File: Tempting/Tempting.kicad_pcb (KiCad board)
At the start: 2 copper layers, 50 parts, among them J1 Conn_Coaxial, J2 Conn_01x07_Socket, J3 Conn_ARM_SWD_TagConnect_TC2030, J4 USB_C_Receptacle_USB2.0_16P, SW1 SPST, SW2 SPST, U1 AMS1117-3.3, U2 SCD41-D-R2, U3 STM32WB55CGUx, U4 DPS368, U5 USBLC6-2SC6, X1 32M, X2 32.768k

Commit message: Added net classes
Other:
- copper layers 2 -> 4
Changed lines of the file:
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@@
 	(generator_version "8.0")
 	(general
-		(thickness 1.6)
+		(thickness 1.5842)
 		(legacy_teardrops no)
 	)
@@
 	(layers
 		(0 "F.Cu" signal)
+		(1 "In1.Cu" signal)
+		(2 "In2.Cu" signal)
 		(31 "B.Cu" signal)
-		(32 "B.Adhes" user "B.Adhesive")
-		(33 "F.Adhes" user "F.Adhesive")
 		(34 "B.Paste" user)
 		(35 "F.Paste" user)
@@
 		(38 "B.Mask" user)
 		(39 "F.Mask" user)
-		(40 "Dwgs.User" user "User.Drawings")
-		(41 "Cmts.User" user "User.Comments")
-		(42 "Eco1.User" user "User.Eco1")
-		(43 "Eco2.User" user "User.Eco2")
 		(44 "Edge.Cuts" user)
 		(45 "Margin" user)
 		(46 "B.CrtYd" user "B.Courtyard")
 		(47 "F.CrtYd" user "F.Courtyard")
-		(48 "B.Fab" user)
-		(49 "F.Fab" user)
-		(50 "User.1" user)
-		(51 "User.2" user)
-		(52 "User.3" user)
-		(53 "User.4" user)
-		(54 "User.5" user)
-		(55 "User.6" user)
-		(56 "User.7" user)
-		(57 "User.8" user)
-		(58 "User.9" user)
 	)
 	(setup
+		(stackup
+			(layer "F.SilkS"
+				(type "Top Silk Screen")
+			)
+			(layer "F.Paste"
+				(type "Top Solder Paste")
+			)
+			(layer "F.Mask"
+				(type "Top Solder Mask")
+				(thickness 0.01)
+			)
+			(layer "F.Cu"
+				(type "copper")
+				(thickness 0.035)
+			)
+			(layer "dielectric 1"
+				(type "prepreg")
+				(thickness 0.0994)
+				(material "3313")
+				(epsilon_r 4.5)
+				(loss_tangent 0.02)
+			)
+			(layer "In1.Cu"
+				(type "copper")
+				(thickness 0.0152)
+			)
+			(layer "dielectric 2"
+				(type "core")
+				(color "FR4 natural")
+				(thickness 1.265)
+				(material "FR4")
+				(epsilon_r 4.5)
+				(loss_tangent 0.02)
+			)
+			(layer "In2.Cu"
+				(type "copper")
+				(thickness 0.0152)
+			)
+			(layer "dielectric 3"
+				(type "prepreg")
+				(thickness 0.0994)
+				(material "3313")
+				(epsilon_r 4.5)
+				(loss_tangent 0.02)
+			)
+			(layer "B.Cu"
+				(type "copper")
+				(thickness 0.035)
+			)
+			(layer "B.Mask"
+				(type "Bottom Solder Mask")
+				(thickness 0.01)
+			)
+			(layer "B.Paste"
+				(type "Bottom Solder Paste")
+			)
+			(layer "B.SilkS"
+				(type "Bottom Silk Screen")
+			)
+			(copper_finish "HAL lead-free")
+			(dielectric_constraints yes)
+		)
 		(pad_to_mask_clearance 0)
 		(allow_soldermask_bridges_in_footprints no)

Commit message: Rough initial layout
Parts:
- added C23: 10u, Capacitor_SMD:C_0805_2012Metric, F.Cu at (110.5, 48.6)
- added C24: 100n, Capacitor_SMD:C_0402_1005Metric, F.Cu at (112.5, 77.5)
- added C25: 100n, Capacitor_SMD:C_0402_1005Metric, F.Cu at (125.5, 77.5)
- C10, C12: value 100n -> 4.7u; footprint Capacitor_SMD:C_0402_1005Metric -> Capacitor_SMD:C_0603_1608Metric
- C11: value C -> 100n
- C13: value 100n -> C
- C17: value 4.7u -> 100n; footprint Capacitor_SMD:C_0603_1608Metric -> Capacitor_SMD:C_0402_1005Metric
- C20: value 10u -> 4.7u; footprint Capacitor_SMD:C_0805_2012Metric -> Capacitor_SMD:C_0603_1608Metric
- moved SW2 99.3 mm to (128.5, 81.8), turned to 180 degrees
- moved FLT1 95.5 mm to (131.9, 60.5)
- moved J2 93.5 mm to (126.1, 45.6), turned to -90 degrees
- moved C6 87.3 mm to (128.5, 63.0), turned to 90 degrees
- moved X1 86.9 mm to (123.8, 52.1)
- moved SW1 86.0 mm to (110.3, 81.8), turned to 180 degrees
- moved R5 84.7 mm to (127.0, 48.6), turned to 180 degrees
- moved L1 84.2 mm to (126.1, 60.5)
- moved C3 84.0 mm to (124.6, 63.0), turned to 90 degrees
- moved U4 82.9 mm to (118.5, 75.5), turned to 90 degrees
- moved C8 82.9 mm to (124.5, 61.1), turned to -90 degrees
- moved J1 82.3 mm to (136.1, 61.0)
- moved C10 81.3 mm to (125.3, 37.7), turned to 90 degrees
- moved R2 81.1 mm to (123.0, 68.5)
- moved C15 80.9 mm to (127.5, 38.3), turned to 90 degrees
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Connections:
- net /MCU_SMPSFB renamed /SMPSFB_MCU
- net /MCU_SMPSLX renamed /SMPSLX_MCU
- net Net-(D1-BK) renamed /LED_B
- net Net-(D1-GK) renamed /LED_G
- net Net-(D1-RK) renamed /LED_R
- net Net-(U3-PA0) renamed /LED_R_MCU
- net Net-(U3-PA1) renamed /LED_G_MCU
- net Net-(U3-PA2) renamed /LED_B_MCU
- C11 pad 1: /LSE_OUT -> +3.3V
- C13 pad 1: +3.3V -> /LSE_OUT
- C21 pad 1: /BUTTON_1 -> +3.3V
- C22 pad 1: /BUTTON_2 -> +3.3V
- SW1 pad 2: unconnected-(SW1-Pad2) -> GND
- SW1 pad 3: unconnected-(SW1-K-Pad3) -> /BUTTON_1
- SW2 pad 2: unconnected-(SW2-Pad2) -> GND
- SW2 pad 3: unconnected-(SW2-K-Pad3) -> /BUTTON_2

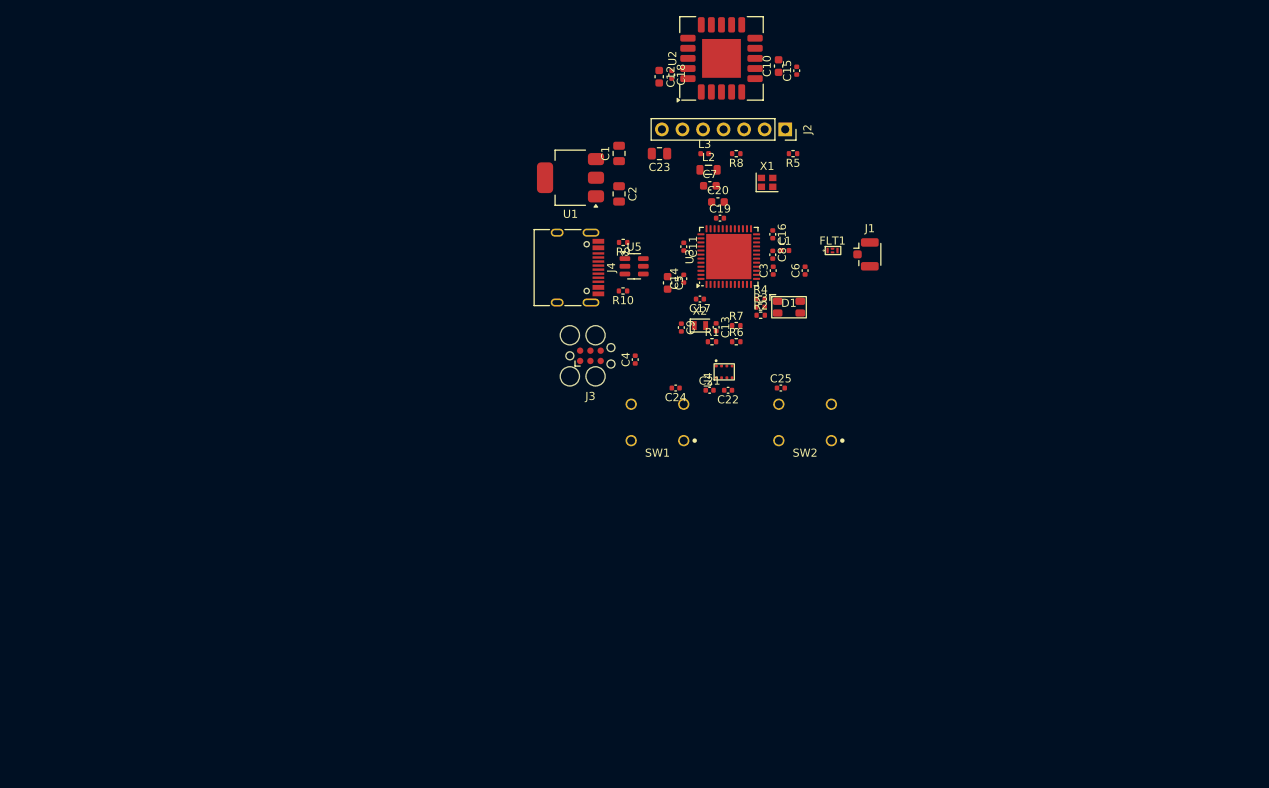
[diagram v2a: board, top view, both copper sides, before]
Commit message: Added edge cuts and mounting holes
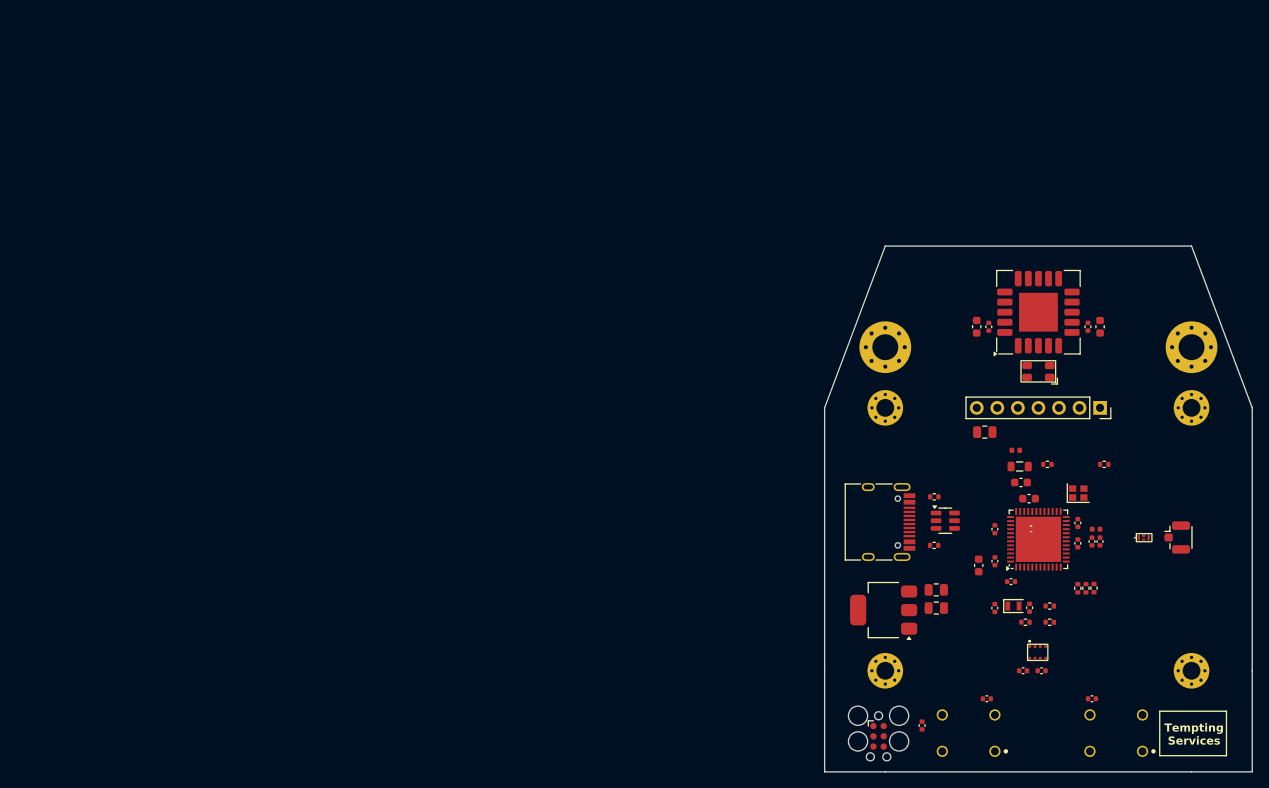
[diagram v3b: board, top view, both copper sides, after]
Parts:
- added H1: MountingHole_Pad, MountingHole:MountingHole_2.2mm_M2_Pad_Via, F.Cu at (176.3, 112.5)
- added H2: MountingHole_Pad, MountingHole:MountingHole_2.2mm_M2_Pad_Via, F.Cu at (176.3, 80.0)
- added H3: MountingHole_Pad, MountingHole:MountingHole_2.2mm_M2_Pad_Via, F.Cu at (138.4, 112.5)
- added H4: MountingHole_Pad, MountingHole:MountingHole_2.2mm_M2_Pad_Via, F.Cu at (138.4, 80.0)
- added H5: MountingHole_Pad, MountingHole:MountingHole_3.2mm_M3_Pad_Via, F.Cu at (138.4, 72.5)
- added H6: MountingHole_Pad, MountingHole:MountingHole_3.2mm_M3_Pad_Via, F.Cu at (176.3, 72.5)
- moved C1 66.7 mm to (144.8, 102.5), turned to 0 degrees
- moved U1 66.0 mm to (138.2, 105.0)
- moved C2 64.5 mm to (144.8, 104.8), turned to 0 degrees
- moved J3 59.0 mm to (137.6, 120.6), turned to -90 degrees
- moved C4 57.5 mm to (143.0, 119.3)
- moved C24 54.4 mm to (151.0, 116.0)
- moved C25 54.4 mm to (164.0, 116.0)
- moved R8 54.4 mm to (158.5, 87.0)
- moved SW1 54.4 mm to (148.8, 120.2)
- moved SW2 54.4 mm to (167.0, 120.2)
- moved X1 54.4 mm to (162.3, 90.5)
- moved C19 54.4 mm to (156.5, 95.0)
- moved R5 54.4 mm to (165.5, 87.0)
- moved R2 53.2 mm to (164.2, 102.3), turned to 90 degrees
- moved R3 53.2 mm to (163.2, 102.3), turned to 90 degrees
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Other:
- board outline added: 52.9 x 65 mm
- board text added: "Tempting Services"

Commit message: Finetuned layout
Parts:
- added C3: 100n, Capacitor_SMD:C_0402_1005Metric, F.Cu at (154.7, 90.3)
- added C7: 100n, Capacitor_SMD:C_0402_1005Metric, F.Cu at (158.6, 101.6)
- added G***: LOGO, LOGO, F.Cu at (170.7, 108.7)
- moved L3 5.86 mm to (156.2, 90.9), turned to 90 degrees
- moved R2 4.64 mm to (159.7, 101.7)
- moved C23 4.48 mm to (157.4, 108.5)
- moved FLT1 4.38 mm to (174.6, 95.0)
- moved J1 4.38 mm to (178.8, 94.9)
- moved C21 4.04 mm to (154.7, 91.3), turned to 180 degrees
- moved U5 3.75 mm to (142.1, 94.0)
- moved C9 3.64 mm to (158.3, 91.1)
- moved R6 3.58 mm to (156.6, 103.7), turned to 180 degrees
- moved R9 3.55 mm to (141.0, 91.5)
- moved R10 3.54 mm to (141.0, 96.4)
- moved C19 3.43 mm to (151.4, 99.2), turned to 90 degrees
- moved C22 3.33 mm to (153.8, 89.0), turned to 180 degrees
- moved C11 3.27 mm to (153.1, 101.7)
- moved C15 3.11 mm to (156.9, 101.7)
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- renumbered C8 to C10, C9 to C11, C10 to C12, C11 to C13, C12 to C14, C13 to C15, C14 to C16, C15 to C17, C16 to C18, C17 to C19, C5 to C2, C18 to C20, C19 to C21, C20 to C22, C21 to C23, C22 to C24, C23 to C25, C24 to C26, C25 to C27, C2 to C4, C3 to C5, C4 to C6, C6 to C8, C7 to C9
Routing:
- added copper zone on In1.Cu, net GND
- added copper zone on In2.Cu, net GND

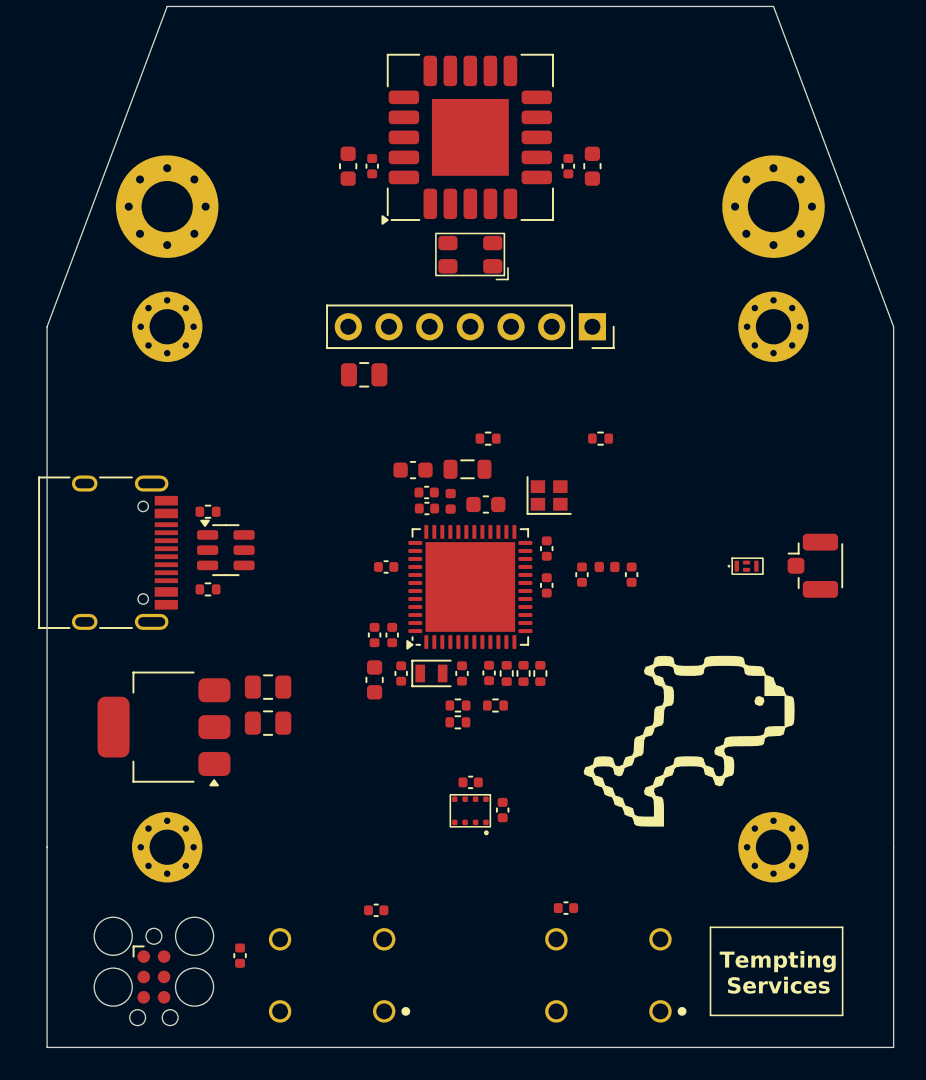
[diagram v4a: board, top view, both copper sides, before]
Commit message: All signal traces routed
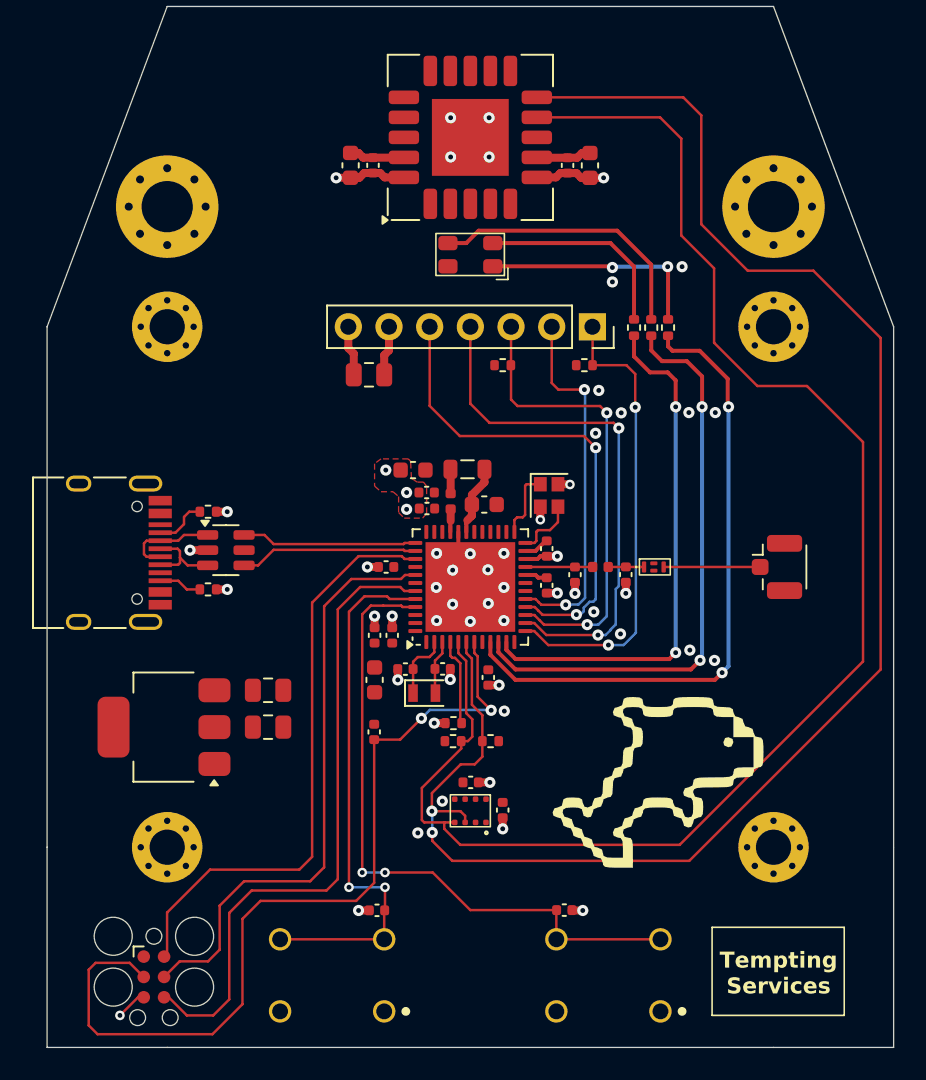
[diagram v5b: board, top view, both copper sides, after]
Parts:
- moved R2 23.8 mm to (169.7, 80.0)
- moved R3 23.0 mm to (168.7, 80.0)
- moved R4 22.4 mm to (167.6, 80.0)
- moved C6 16.3 mm to (151.4, 105.3)
- moved FLT1 5.79 mm to (168.8, 95.0)
- moved R5 4.69 mm to (164.5, 82.4), turned to 0 degrees
- moved R8 4.67 mm to (159.4, 82.4)
- moved C8 3.54 mm to (163.9, 95.5)
- moved G*** 3.22 mm to (168.8, 111.3)
- moved C5 2.74 mm to (167.1, 95.5)
- moved R6 2.25 mm to (156.3, 105.9)
- moved R7 2.25 mm to (158.6, 105.9)
- moved J1 2.24 mm to (176.5, 95.0)
- moved X2 1.31 mm to (154.5, 102.9)
- moved C15 1.24 mm to (155.7, 101.4), turned to 0 degrees
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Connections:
- U3 pad 28: /BUTTON_1 -> unconnected-(U3-PB0-Pad28)
- U3 pad 29: /BUTTON_2 -> unconnected-(U3-PB1-Pad29)
- U3 pad 44: unconnected-(U3-PB4-Pad44) -> /BUTTON_1
- U3 pad 45: unconnected-(U3-PB5-Pad45) -> /BUTTON_2
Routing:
- net /SENSORS_SDA: track 0.00 -> 103.1 mm, vias 0 -> 2
- net /SENSORS_SCL: track 0.00 -> 95.6 mm
- net /SWD_NRST: track 0.00 -> 54.3 mm, vias 0 -> 2
- net /BUTTON_2: track 0.00 -> 41.1 mm, vias 0 -> 2
- net /SWD_SWO: track 0.00 -> 40.4 mm
- net /LED_R_MCU: track 0.00 -> 39.9 mm, vias 0 -> 2
- net /SWD_CLK: track 0.00 -> 37.2 mm
- net /SWD_DIO: track 0.00 -> 36.9 mm
- net /LED_G_MCU: track 0.00 -> 36.5 mm, vias 0 -> 2
- net /BUTTON_1: track 0.00 -> 33.8 mm, vias 0 -> 2
- net GND: track 0.00 -> 33.7 mm, vias 0 -> 56
- net /OLED_CLK: track 0.00 -> 33.3 mm, vias 0 -> 2
- net /LED_B_MCU: track 0.00 -> 33.0 mm, vias 0 -> 2
- net /OLED_DIN: track 0.00 -> 31.0 mm, vias 0 -> 2
- net /OLED_NCS: track 0.00 -> 29.1 mm, vias 0 -> 2
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- added copper zone on F.Cu, net GND

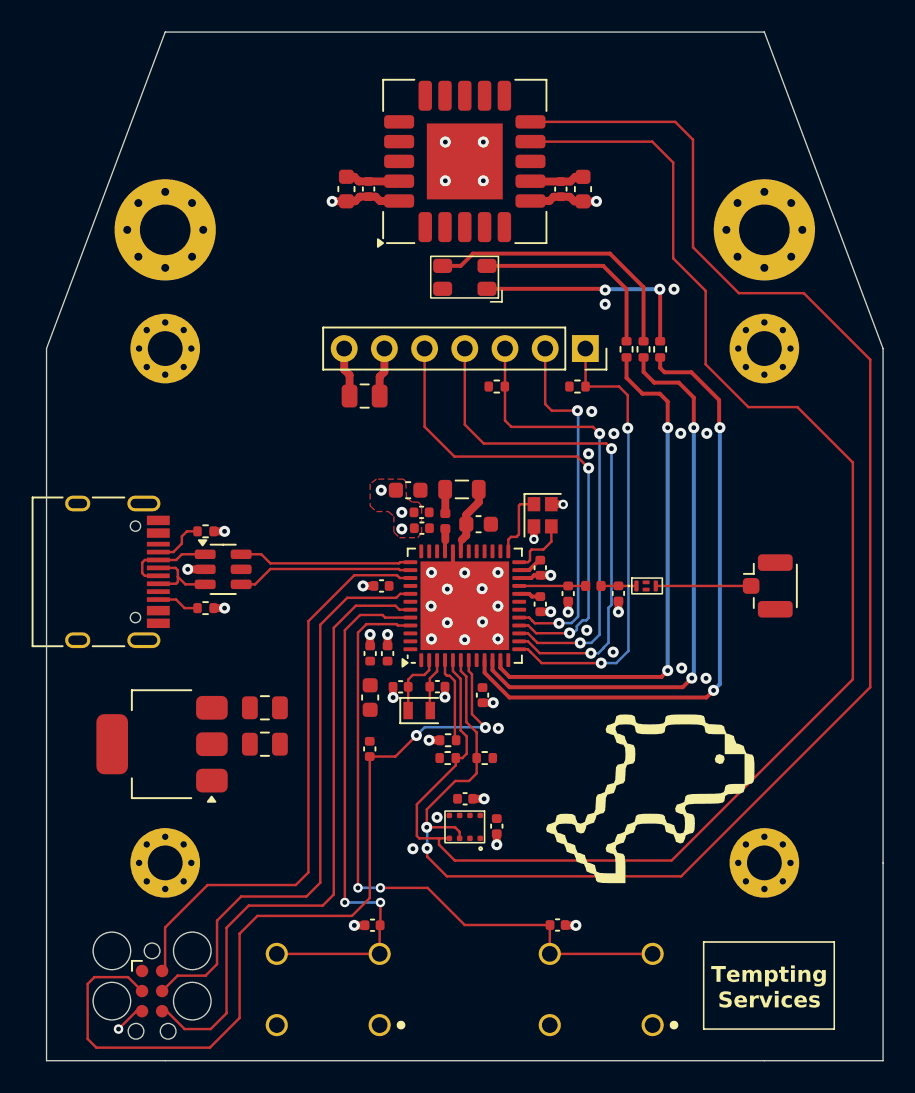
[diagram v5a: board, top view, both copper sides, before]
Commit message: Fixed DRC violations
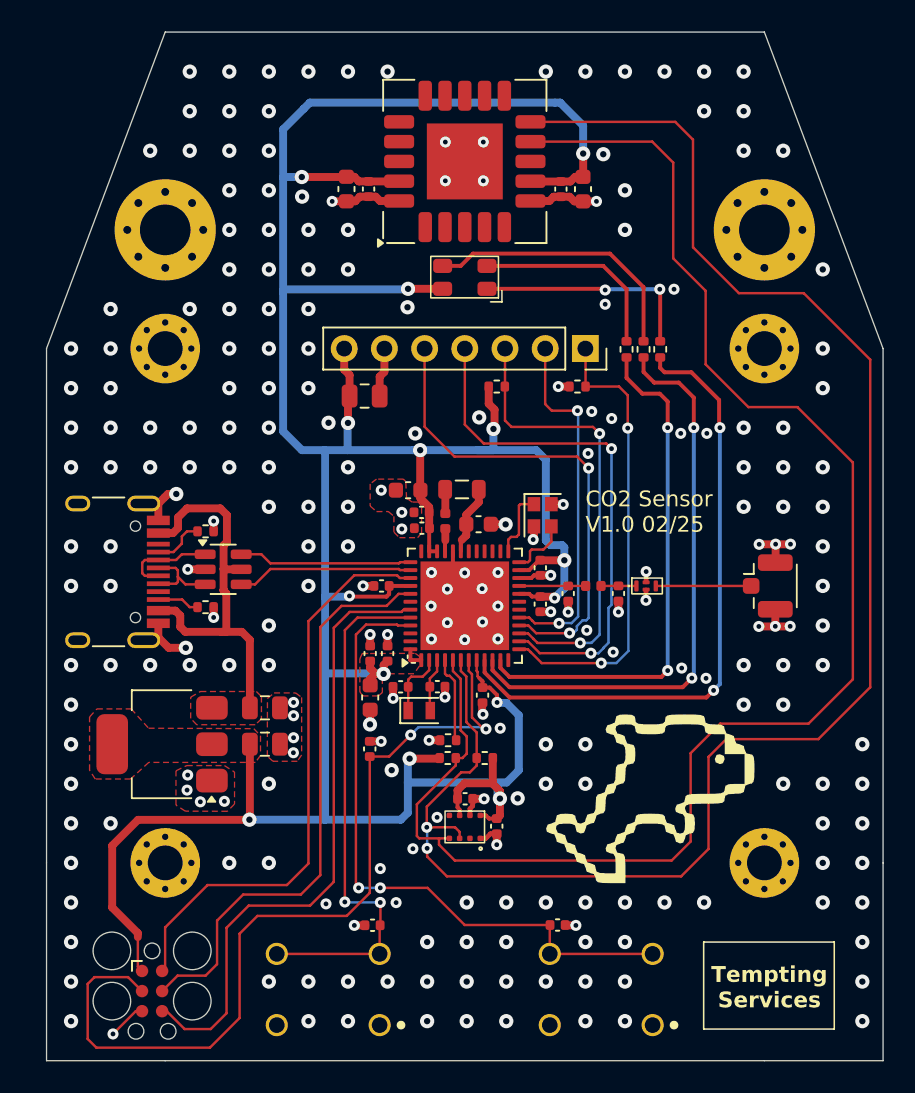
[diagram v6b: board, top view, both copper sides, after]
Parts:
- moved R10 0.06 mm to (141.0, 96.3)
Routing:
- net +3.3V: track 13.0 -> 218.5 mm, vias 0 -> 14
- net VBUS: track 0.00 -> 25.5 mm
- net GND: track 33.7 -> 52.8 mm, vias 56 -> 247
- net /SENSORS_SCL: track 95.6 -> 98.8 mm
- net /SENSORS_SDA: track 103.1 -> 106.3 mm
- net /SWD_SWO: track 40.4 -> 39.7 mm
- added copper zone on F.Cu, net +3.3V
- added copper zone on F.Cu, net VBUS
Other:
- board text added: "CO2 Sensor V1.0 02/25"
